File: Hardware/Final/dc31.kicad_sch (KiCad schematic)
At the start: 73 parts, among them J2 MIDI IN, J2 Micro_SD_Card_SPI, J3 MIDI OUT, J5 SYNC OUT, J6 SYNC IN, J7 HEADPHONE, J7 OLED, J8 Eurorack, Q1 3904, SW1 SW_Push, SW10 SW_Push, SW12 SW_Push, SW2 SW_Push, SW3 SW_Push, SW5 SW_Push, SW6 SW_Push, SW7 Rotary, SW7 SW_Push, SW8 SW_Push, SW9 SW_Push, U1 Pico, U2 MAX98357A/B, U3 74HC04, U4 TPS61023, U5 TLP2361, U6 TPS62153, U8 OPA341UA

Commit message: Update schematic and flesh out BOM with parts
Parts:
- removed BT1, BT2: Battery, symbol Device:Battery
- removed C5: 10uF, symbol Device:C
- removed C6, C7: 22uF, symbol Device:C
- removed L1: 1uH, symbol Device:L_Small
- removed R12: 100k, symbol Device:R
- removed R5: 732k, symbol Device:R
- removed U4: TPS61023, Package_TO_SOT_SMD:SOT-563, symbol TPS61023:TPS61023
- added J7: FRONT, lib_fp:OLED, symbol Connector_Generic:Conn_01x04
- added SW13: Battery Power, symbol Switch:SW_SPST
- added TP2: BATT+, TestPoint:TestPoint_Pad_1.5x1.5mm, symbol Connector:TestPoint
- added TP3: BATT-, TestPoint:TestPoint_Pad_1.5x1.5mm, symbol Connector:TestPoint
- C2: renamed from C8; footprint (none) -> Capacitor_SMD:C_0603_1608Metric
- C3: renamed from C9; footprint (none) -> Capacitor_SMD:C_0603_1608Metric
- J7: renamed from J8; footprint (none) -> Connector_IDC:IDC-Header_2x05_P2.54mm_Horizontal
- R11: renamed from R13; footprint (none) -> Resistor_SMD:R_0603_1608Metric
- SW1: value SW_Push -> Seq1
- SW10: renamed from SW12; value SW_Push -> Function
- SW2: value SW_Push -> Seq2
- SW3: value SW_Push -> Seq3
- SW4: renamed from SW5; value SW_Push -> Seq4
- SW5: renamed from SW6; value SW_Push -> Seq5
- SW6: renamed from SW7; value SW_Push -> Seq6
- SW7: value Rotary -> Volume
- SW7: value Rotary -> Function Select
- SW7: renamed from SW8; value SW_Push -> Seq7
- SW8: renamed from SW9; value SW_Push -> Seq8
- SW9: renamed from SW10; value SW_Push -> PlayPause
- renumbered C4 to C1, C2 to C5, C3 to C6, D14 to D13, D15 to D14, D16 to D15, D13 to D16, J5 to J2, J6 to J4, J2 to J5, J3 to J6, J7 to J8, L2 to L1, R6 to R1, R2 to R10, R7 to R2, R8 to R3, R9 to R4, R10 to R5, R11 to R6, R1 to R7, R4 to R8, R3 to R9, TP3 to TP1, TP2 to TP4, TP1 to TP5, U8 to U2, U2 to U3, U3 to U4
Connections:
- net +3V3: now also J7.2 (Pin_2)
- net GND: now also J7.1 (Pin_1), TP3.1
- net VCC: now reaches D14.1 (K), D15.1 (K), U1.39 (VSYS)
- net at D15.2 (A): now also SW13.1 (A)
- net at J8.3, U3.10 (OUTN): now also J8.2; no longer J8.4
- net at TP5.1: now also J8.4; no longer J8.2
- net RGB_IN renamed RGB
- net RGB: now also J7.4 (Pin_4)
- new net: SW13.2 (B), TP2.1
- no-connect marks 10 -> 21
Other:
- note added: "Front Board"
- note added: "Power Selection"
- note removed: "Fix This"
- note removed: "MIDI needs UART pins"
- note removed: "Probably not populated"
- moved on the sheet: C1, C2, C3, C5, C6, D1, D10, D11, D12, D13, D14, D15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

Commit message: Schematic is pretty much complete.  Back board is 90% routed.
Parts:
- removed SW13: Battery Power, symbol Switch:SW_SPST
- added C7: 22uF, Capacitor_SMD:C_0805_2012Metric, symbol Device:C
- added SW14: SW_SPDT, lib_fp:SW_SPDT_CK-JS102011SAQN, symbol Switch:SW_SPDT
- C2, C3: footprint Capacitor_SMD:C_0603_1608Metric -> Capacitor_SMD:C_0805_2012Metric
- D1, D10, D11, D12, D13, D16, D2, D3, D4, D5, D6, D7, D8, D9: footprint Diode_SMD:D_SOD-123 -> Diode_SMD:D_SOD-323
- D14, D15: footprint (none) -> Diode_SMD:D_SOD-323
- J7: footprint lib_fp:OLED -> Connector_PinHeader_2.54mm:PinHeader_1x04_P2.54mm_Vertical
- J7: footprint Connector_IDC:IDC-Header_2x05_P2.54mm_Horizontal -> Connector_IDC:IDC-Header_2x05_P2.54mm_Vertical
- L1: footprint (none) -> Inductor_SMD:L_Wuerth_MAPI-3015
- Q1: symbol Device:Q_NPN_EBC -> Device:Q_NPN_BEC
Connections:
- net +5V: now also C7.1; no longer U2.7 (V+), U2.8 (~{SHDN})
- net C0: now also SW4.1
- net C1: now also SW7.1, SW8.1; no longer SW4.1
- net C2: now also SW10.1, SW7.S2, SW7.S2, U1.24 (GPIO18); no longer SW7.1, SW8.1, U1.29 (GPIO22)
- net GND: now also Q1.2 (E), C7.2; no longer Q1.1 (E)
- net R0: now also D5.1 (K), D9.1 (K); no longer D10.1 (K), D4.1 (K), D7.1 (K)
- net R1: now also D10.1 (K), D6.1 (K), U1.27 (GPIO21); no longer D11.1 (K), D5.1 (K), D8.1 (K), U1.25 (GPIO19)
- net R2: now also D11.1 (K), D7.1 (K), U1.29 (GPIO22); no longer D12.1 (K), D6.1 (K), D9.1 (K), U1.24 (GPIO18)
- net RGB: now also U1.5 (GPIO3); no longer U1.34 (GPIO28_ADC2)
- net SCL: now also U1.20 (GPIO15); no longer U1.19 (GPIO14)
- net SDA: now also U1.19 (GPIO14); no longer U1.20 (GPIO15)
- net VCC: now also U2.7 (V+), U2.8 (~{SHDN})
- net at D13.1 (K), R5.2: now also Q1.1 (B); no longer Q1.2 (B)
- net at TP2.1: now also SW14.2 (B)
- net at D15.2 (A): now also SW14.3 (C)
- removed net C3: SW10.1, SW7.S2, SW7.S2, U1.27 (GPIO21)
- new net R3: D12.1 (K), D4.1 (K), D8.1 (K), U1.34 (GPIO28_ADC2)
- no-connect marks 21 -> 20
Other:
- note removed: "Uses 5V"
- moved on the sheet: C2, C3, D1, D10, D11, D12, D14, D15, D2, D3, D4, D5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

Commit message: Almost final, still need some artwork
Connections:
- net ENC1_A: now also U1.21 (GPIO16); no longer U1.6 (GPIO4)
- net ENC1_B: now also U1.22 (GPIO17); no longer U1.7 (GPIO5)
- net ENC2_A: now also U1.6 (GPIO4); no longer U1.22 (GPIO17)
- net ENC2_B: now also U1.7 (GPIO5); no longer U1.21 (GPIO16)
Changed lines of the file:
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@@
     )
   )
-  (global_label "ENC2_B" (shape input) (at 181.864 103.886 0)
-    (effects (font (size 1.27 1.27)) (justify left))
-    (property "Intersheetrefs" "${INTERSHEET_REFS}" (at 181.864 103.886 0)
+  (global_label "ENC2_B" (shape input) (at 133.604 70.866 180)
+    (effects (font (size 1.27 1.27)) (justify right))
+    (property "Intersheetrefs" "${INTERSHEET_REFS}" (at 133.604 70.866 0)
       (effects (font (size 1.27 1.27)) hide)
     )
   )
-  (global_label "ENC1_B" (shape input) (at 133.604 70.866 180)
-    (effects (font (size 1.27 1.27)) (justify right))
-    (property "Intersheetrefs" "${INTERSHEET_REFS}" (at 133.604 70.866 0)
+  (global_label "ENC1_B" (shape input) (at 181.864 101.346 0)
+    (effects (font (size 1.27 1.27)) (justify left))
+    (property "Intersheetrefs" "${INTERSHEET_REFS}" (at 181.864 101.346 0)
       (effects (font (size 1.27 1.27)) hide)
     )
@@
     )
   )
-  (global_label "ENC1_A" (shape input) (at 133.604 68.326 180)
-    (effects (font (size 1.27 1.27)) (justify right))
-    (property "Intersheetrefs" "${INTERSHEET_REFS}" (at 133.604 68.326 0)
+  (global_label "ENC1_A" (shape input) (at 181.864 103.886 0)
+    (effects (font (size 1.27 1.27)) (justify left))
+    (property "Intersheetrefs" "${INTERSHEET_REFS}" (at 181.864 103.886 0)
       (effects (font (size 1.27 1.27)) hide)
     )
@@
     )
   )
-  (global_label "ENC2_A" (shape input) (at 181.864 101.346 0)
-    (effects (font (size 1.27 1.27)) (justify left))
-    (property "Intersheetrefs" "${INTERSHEET_REFS}" (at 181.864 101.346 0)
+  (global_label "ENC2_A" (shape input) (at 133.604 68.326 180)
+    (effects (font (size 1.27 1.27)) (justify right))
+    (property "Intersheetrefs" "${INTERSHEET_REFS}" (at 133.604 68.326 0)
       (effects (font (size 1.27 1.27)) hide)
     )

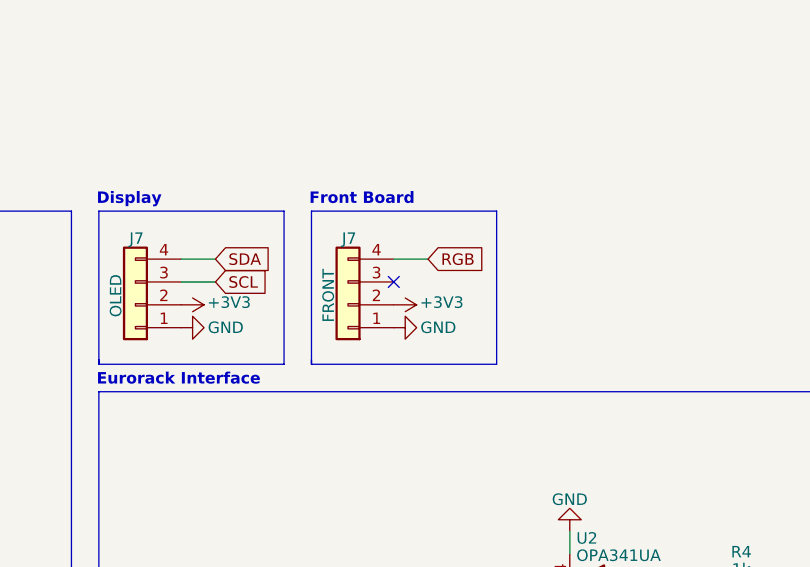
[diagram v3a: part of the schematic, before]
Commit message: Adding SAO port to front panel Adding hamster art to boards A few more small tweaks before final export
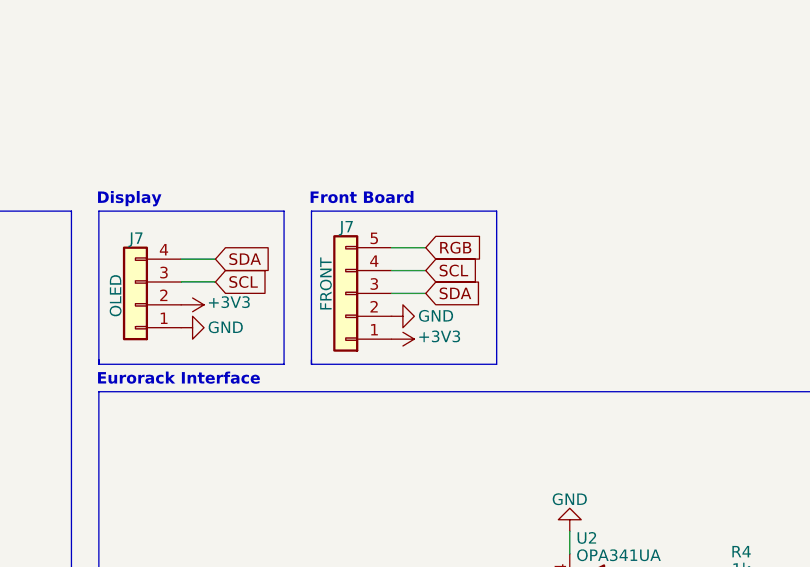
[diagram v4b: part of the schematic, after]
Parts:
- J7: footprint Connector_PinHeader_2.54mm:PinHeader_1x04_P2.54mm_Vertical -> Connector_PinHeader_2.54mm:PinHeader_1x05_P2.54mm_Vertical; symbol Connector_Generic:Conn_01x04 -> Connector_Generic:Conn_01x05
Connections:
- net +3V3: now also J7.1 (Pin_1); no longer J7.2 (Pin_2)
- net GND: now also J7.2 (Pin_2); no longer J7.1 (Pin_1)
- net RGB: now also J7.5 (Pin_5); no longer J7.4 (Pin_4)
- net SCL: now also J7.4 (Pin_4)
- net SDA: now also J7.3 (Pin_3)
- no-connect marks 20 -> 19
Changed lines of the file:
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@@
   (no_connect (at 252.73 207.01))
   (no_connect (at 313.69 92.71))
-  (no_connect (at 173.228 152.654))
   (no_connect (at 323.596 164.084))
   (no_connect (at 323.596 132.334))
@@
     (stroke (width 0) (type default))
   )
-  (wire (pts (xy 177.038 150.114) (xy 173.228 150.114))
+  (wire (pts (xy 176.784 148.844) (xy 172.974 148.844))
     (stroke (width 0) (type default))
   )
@@
     (stroke (width 0) (type default))
   )
+  (wire (pts (xy 172.974 151.384) (xy 176.784 151.384))
+    (stroke (width 0) (type default))
+  )
   (wire (pts (xy 373.888 41.148) (xy 376.428 41.148))
     (stroke (width 0) (type default))
   )
+  (wire (pts (xy 172.974 153.924) (xy 176.784 153.924))
+    (stroke (width 0) (type default))
+  )
   (wire (pts (xy 86.106 160.274) (xy 97.536 160.274))
     (stroke (width 0) (type default))
@@
     )
   )
+  (global_label "SDA" (shape input) (at 176.784 153.924 0)
+    (effects (font (size 1.27 1.27)) (justify left))
+    (property "Intersheetrefs" "${INTERSHEET_REFS}" (at 176.784 153.924 0)
+      (effects (font (size 1.27 1.27)) hide)
+    )
+  )
   (global_label "I2S_DIN" (shape input) (at 328.422 219.202 180)
     (effects (font (size 1.27 1.27)) (justify right))
@@
     )
   )
+  (global_label "SCL" (shape input) (at 176.784 151.384 0)
+    (effects (font (size 1.27 1.27)) (justify left))
+    (property "Intersheetrefs" "${INTERSHEET_REFS}" (at 176.784 151.384 0)
+      (effects (font (size 1.27 1.27)) hide)
+    )
+  )
   (global_label "SYNC_OUT" (shape input) (at 218.186 186.69 0) (fields_autoplaced)
     (effects (font (size 1.27 1.27)) (justify left))
@@
     )
   )
-  (global_label "RGB" (shape input) (at 177.038 150.114 0)
+  (global_label "RGB" (shape input) (at 176.784 148.844 0)
     (effects (font (size 1.27 1.27)) (justify left))
-    (property "Intersheetrefs" "${INTERSHEET_REFS}" (at 177.038 150.114 0)
+    (property "Intersheetrefs" "${INTERSHEET_REFS}" (at 176.784 148.844 0)
       (effects (font (size 1.27 1.27)) hide)
     )
@@
     )
   )
-  (symbol (lib_id "Connector_Generic:Conn_01x04") (at 168.148 155.194 180) (unit 1)
+  (symbol (lib_id "Connector_Generic:Conn_01x05") (at 167.894 153.924 180) (unit 1)
     (in_bom yes) (on_board yes) (dnp no)
-    (property "Reference" "J7" (at 168.275 147.828 0)
+    (property "Reference" "J7" (at 168.021 146.558 0)
       (effects (font (size 1.27 1.27)))
     )
-    (property "Value" "FRONT" (at 165.989 154.178 90)
+    (property "Value" "FRONT" (at 165.735 152.908 90)
       (effects (font (size 1.27 1.27)))
     )
-    (property "Footprint" "Connector_PinHeader_2.54mm:PinHeader_1x04_P2.54mm_Vertical" (at 168.148 155.194 0)
+    (property "Footprint" "Connector_PinHeader_2.54mm:PinHeader_1x05_P2.54mm_Vertical" (at 167.894 153.924 0)
       (effects (font (size 1.27 1.27)) hide)
     )
-    (property "Datasheet" "~" (at 168.148 155.194 0)
+    (property "Datasheet" "~" (at 167.894 153.924 0)
       (effects (font (size 1.27 1.27)) hide)
     )
@@
     (pin "3")
     (pin "4")
+    (pin "5")
     (instances
       (project "laser-theremin"
@@
     )
   )
-  (symbol (lib_id "power:+3V3") (at 173.228 155.194 270) (unit 1)
+  (symbol (lib_id "power:+3V3") (at 172.974 159.004 270) (unit 1)
     (in_bom yes) (on_board yes) (dnp no)
-    (property "Reference" "#PWR0134" (at 169.418 155.194 0)
+    (property "Reference" "#PWR0134" (at 169.164 159.004 0)
       (effects (font (size 1.27 1.27)) hide)
     )
-    (property "Value" "+3V3" (at 178.562 154.94 90)
+    (property "Value" "+3V3" (at 178.308 158.75 90)
       (effects (font (size 1.27 1.27)))
     )
-    (property "Footprint" "" (at 173.228 155.194 0)
+    (property "Footprint" "" (at 172.974 159.004 0)
       (effects (font (size 1.27 1.27)) hide)
     )
-    (property "Datasheet" "" (at 173.228 155.194 0)
+    (property "Datasheet" "" (at 172.974 159.004 0)
       (effects (font (size 1.27 1.27)) hide)
     )
@@
     )
   )
-  (symbol (lib_id "power:GND") (at 173.228 157.734 90) (unit 1)
+  (symbol (lib_id "power:GND") (at 172.974 156.464 90) (unit 1)
     (in_bom yes) (on_board yes) (dnp no)
-    (property "Reference" "#PWR0135" (at 179.578 157.734 0)
+    (property "Reference" "#PWR0135" (at 179.324 156.464 0)
       (effects (font (size 1.27 1.27)) hide)
     )
-    (property "Value" "GND" (at 178.181 157.734 90)
+    (property "Value" "GND" (at 177.927 156.464 90)
       (effects (font (size 1.27 1.27)))
     )
-    (property "Footprint" "" (at 173.228 157.734 0)
+    (property "Footprint" "" (at 172.974 156.464 0)
       (effects (font (size 1.27 1.27)) hide)
     )
-    (property "Datasheet" "" (at 173.228 157.734 0)
+    (property "Datasheet" "" (at 172.974 156.464 0)
       (effects (font (size 1.27 1.27)) hide)
     )

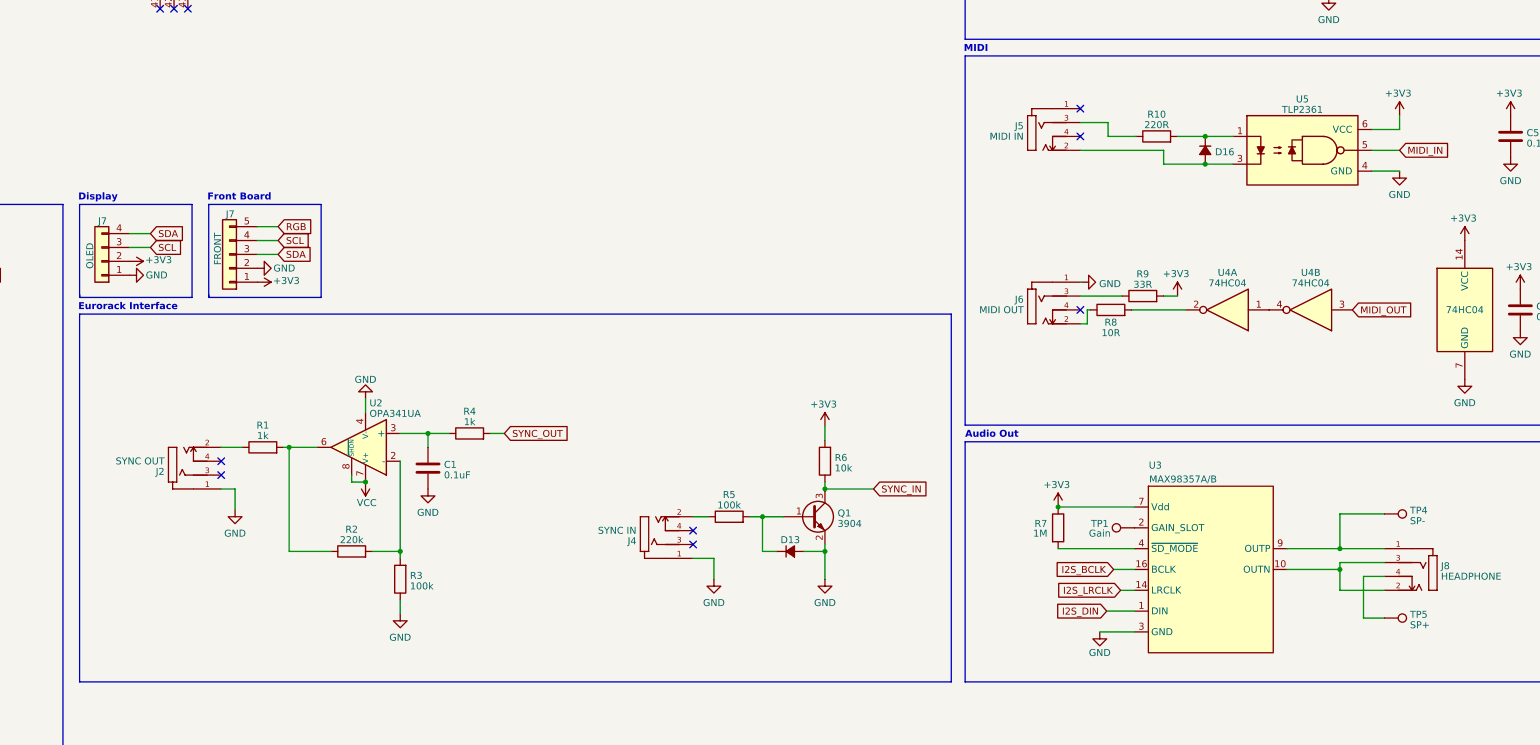
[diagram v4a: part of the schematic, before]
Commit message: Generated 1.1 rev to switch to KYCON 3.5mm jacks due to parts issues with the Molex
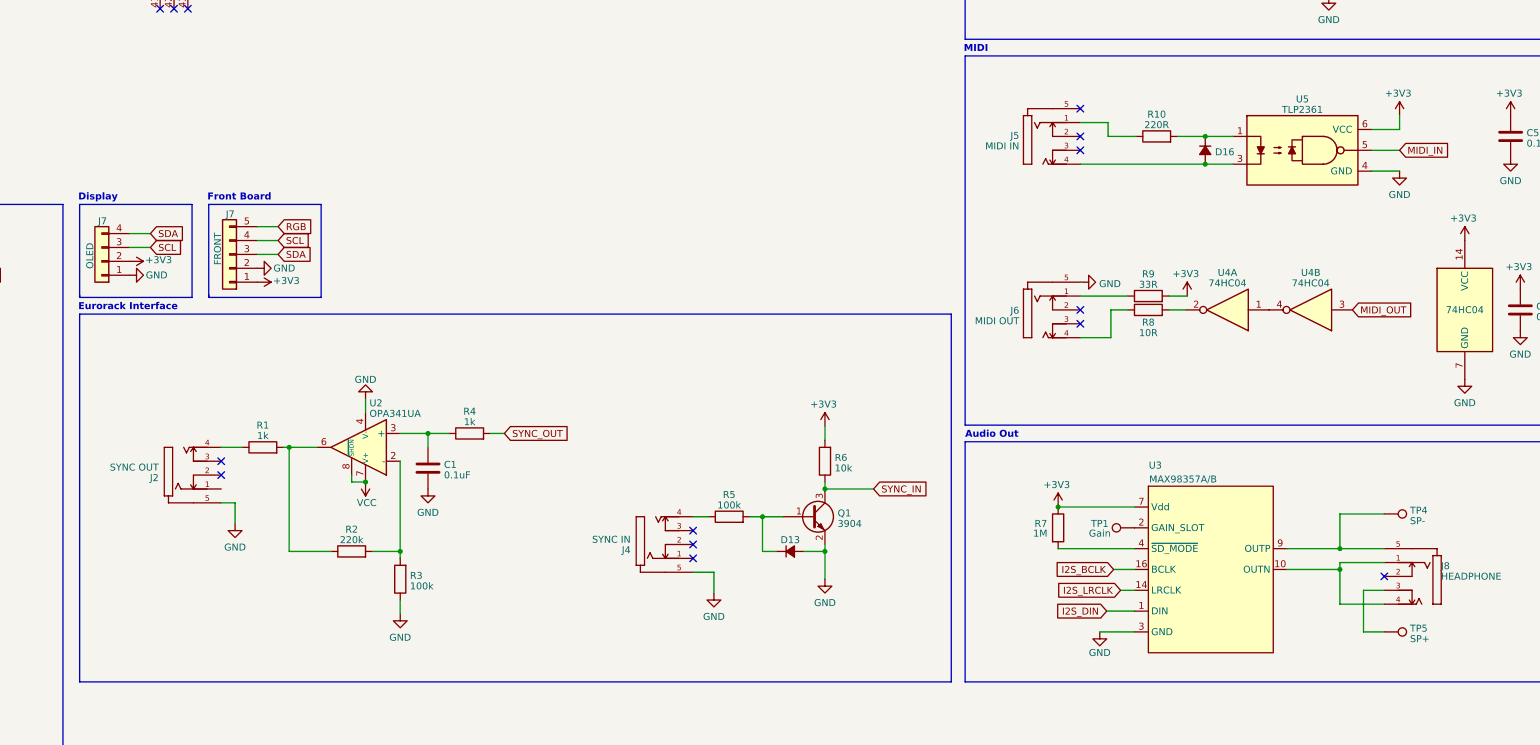
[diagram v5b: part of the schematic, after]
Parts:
- J2, J4, J5, J6, J8: footprint lib_fp:MOLEX_47257-0001 -> lib_fp:STX-3790-5N; symbol 47257-0001:47257-0001 -> STX-3790-5N:STX-3790-5N; MANUFACTURER Molex -> KYCON
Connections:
- net GND: now also J2.5, J4.5, J6.5; no longer J2.1, J4.1, J6.1
- net at R1.1: now also J2.4; no longer J2.2
- net at R5.1: now also J4.4; no longer J4.2
- net at TP4.1, U3.9 (OUTP): now also J8.5; no longer J8.1
- net at J5.1: now also R10.1
- net at D16.2 (A), U5.3: now also J5.4; no longer J5.2
- net at J5.3: no longer R10.1
- net at J6.2: no longer R8.1
- net at R9.1: now also J6.1; no longer J6.3
- net at J6.4: now also R8.1
- net at J8.4: now also J8.1, U3.10 (OUTN); no longer TP5.1
- new net: J8.3, TP5.1
- now unconnected: J8.2
- no-connect marks 19 -> 23
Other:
- title: DC31 Syth Badge -> DC31 Electic Sampler Badge
- moved on the sheet: R8, R9, TP5
